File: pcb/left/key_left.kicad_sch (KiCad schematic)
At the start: 106 parts, among them J1 Conn01_02, J3 USB_C_Receptacle_USB2.0_16P, J4 Conn_01x06_Socket, J5 Conn_01x04_Pin, SW1 SW_Push, SW10 SW_Push, SW11 SW_Push, SW12 SW_Push, SW13 SW_Push, SW14 SW_Push, SW15 SW_Push, SW16 SW_Push, SW17 SW_Push, SW18 SW_Push, SW19 SW_Push, SW2 SW_Push, SW20 SW_Push, SW21 SW_Push, SW22 SW_Push, SW23 SW_Push, SW3 SW_Push, SW4 SW_Push, SW5 SW_Push, SW6 SW_Push, SW7 SW_Push, SW8 SW_Push, SW9 SW_Push, U2 MDBT50Q-1MV2, U3 IS31FL3733-TQ, U4 BQ24074RGT

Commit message: ERC verified and symbols are added
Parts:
- C29, C30, C31, C6, C8, C9: footprint (none) -> Capacitor_SMD:C_0805_2012Metric
- D24, D25, D26, D27, D28, D30, D31, D32, D33, D34, D36, D37, D38, D39, D40, D41, D42, D43, D44, D45, D46, D47, D48, D50: footprint (none) -> LED_SMD:LED_RGB_5050-6; symbol Device:LED_RGB -> LED_RGB_5050:LED_RGB_5050
- R1, R10, R11, R12, R13, R14, R15, R16, R17, R18, R19, R4, R7, R8, R9: footprint (none) -> Resistor_SMD:R_0805_2012Metric
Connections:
- net CS1: now also D24.2 (RK), D30.2 (RK), D36.2 (RK), D41.2 (RK), D46.2 (RK); no longer D24.1 (RK), D30.1 (RK), D36.1 (RK), D41.1 (RK), D46.1 (RK)
- net CS10: now also D27.2 (RK), D33.2 (RK), D39.2 (RK), D44.2 (RK); no longer D27.1 (RK), D33.1 (RK), D39.1 (RK), D44.1 (RK)
- net CS11: now also D27.3 (GK), D33.3 (GK), D39.3 (GK), D44.3 (GK); no longer D27.2 (GK), D33.2 (GK), D39.2 (GK), D44.2 (GK)
- net CS12: now also D27.1 (BK), D33.1 (BK), D39.1 (BK), D44.1 (BK); no longer D27.3 (BK), D33.3 (BK), D39.3 (BK), D44.3 (BK)
- net CS13: now also D28.2 (RK), D34.2 (RK), D40.2 (RK), D45.2 (RK); no longer D28.1 (RK), D34.1 (RK), D40.1 (RK), D45.1 (RK)
- net CS14: now also D28.3 (GK), D34.3 (GK), D40.3 (GK), D45.3 (GK); no longer D28.2 (GK), D34.2 (GK), D40.2 (GK), D45.2 (GK)
- net CS15: now also D28.1 (BK), D34.1 (BK), D40.1 (BK), D45.1 (BK); no longer D28.3 (BK), D34.3 (BK), D40.3 (BK), D45.3 (BK)
- net CS2: now also D24.3 (GK), D30.3 (GK), D36.3 (GK), D41.3 (GK), D46.3 (GK); no longer D24.2 (GK), D30.2 (GK), D36.2 (GK), D41.2 (GK), D46.2 (GK)
- net CS3: now also D24.1 (BK), D30.1 (BK), D36.1 (BK), D41.1 (BK), D46.1 (BK); no longer D24.3 (BK), D30.3 (BK), D36.3 (BK), D41.3 (BK), D46.3 (BK)
- net CS4: now also D25.2 (RK), D31.2 (RK), D37.2 (RK), D42.2 (RK), D47.2 (RK); no longer D25.1 (RK), D31.1 (RK), D37.1 (RK), D42.1 (RK), D47.1 (RK)
- net CS5: now also D25.3 (GK), D31.3 (GK), D37.3 (GK), D42.3 (GK), D47.3 (GK); no longer D25.2 (GK), D31.2 (GK), D37.2 (GK), D42.2 (GK), D47.2 (GK)
- net CS6: now also D25.1 (BK), D31.1 (BK), D37.1 (BK), D42.1 (BK), D47.1 (BK); no longer D25.3 (BK), D31.3 (BK), D37.3 (BK), D42.3 (BK), D47.3 (BK)
- net CS7: now also D26.2 (RK), D32.2 (RK), D38.2 (RK), D43.2 (RK), D48.2 (RK); no longer D26.1 (RK), D32.1 (RK), D38.1 (RK), D43.1 (RK), D48.1 (RK)
- net CS8: now also D26.3 (GK), D32.3 (GK), D38.3 (GK), D43.3 (GK), D48.3 (GK); no longer D26.2 (GK), D32.2 (GK), D38.2 (GK), D43.2 (GK), D48.2 (GK)
- net CS9: now also D26.1 (BK), D32.1 (BK), D38.1 (BK), D43.1 (BK), D48.1 (BK); no longer D26.3 (BK), D32.3 (BK), D38.3 (BK), D43.3 (BK), D48.3 (BK)
- net GND: now also J3.SH (SHIELD); no longer J3.S1 (SHIELD)
- net at R16.1: now also D50.2 (RK); no longer D50.1 (RK)
- net at R14.1: now also D50.1 (BK); no longer D50.3 (BK)
- net at R15.2: now also D50.3 (GK); no longer D50.2 (GK)
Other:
- moved on the sheet: C6, C8, C9, J3, R11, R12, R13, R17, R18, R19, R2, R3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

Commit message: SWD firmware debug unit added
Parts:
- added C1: 1uF, symbol Device:C
- added C2, C3, C4: 100nF, symbol Device:C
- added C5: C, symbol Device:C
- added LDO1: ME6211C33M5G-N, easyeda2kicad:SOT-23-5_L3.0-W1.7-P0.95-LS2.8-BL, symbol easyeda2kicad:ME6211C33M5G-N
- added Q1: AO3401A, easyeda2kicad:SOT-23_L2.9-W1.3-P1.90-LS2.4-BR, symbol easyeda2kicad:AO3401A
- added Q2: 2N7002, easyeda2kicad:SOT-23-3_L2.9-W1.3-P1.90-LS2.4-BR, symbol easyeda2kicad:2N7002
- added R20: 100 k, symbol Device:R
- added R21, R22: 100k, symbol Device:R
- added SW24: SW_Push, symbol Switch:SW_Push
- added U1: CH552E, easyeda2kicad:MSOP-10_L3.0-W3.0-P0.50-LS5.0-BL, symbol easyeda2kicad:CH552E
- added U5: FSUSB42UMX-TP, easyeda2kicad:XQFN-10_L1.8-W1.4-P0.40-TL, symbol easyeda2kicad:FSUSB42UMX-TP
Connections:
- net +5V: now also C3.2, LDO1.1 (VIN), LDO1.3 (CE), Q1.2 (S), R21.2
- net GND: now also C1.1, C2.1, C3.1, C4.2, C5.2, LDO1.2 (VSS), Q1.3 (D), Q2.1 (G), Q2.2 (S), R20.2, R22.2, SW24.2, U1.8 (GND/VSS), U5.3 (GND), U5.8 (~{OE})
- net USB_D+: now also U5.1 (D+); no longer U2.35 (D+)
- net USB_D-: now also U5.2 (D-); no longer U2.34 (D-)
- net NRST: now reaches U2.40 (P0.18)
- net NRST: now also U1.3 (P1.6/MISO/RXD1/TIN4)
- net at J5.1 (Pin_1): no longer U2.51 (SWDIO)
- net at J5.2 (Pin_2): no longer U2.53 (SWDCLK)
- new net: R22.1, U1.4 (P1.7/SCK/TXD1/TIN5)
- new net: C4.1, U1.9 (VCC/VDD)
- new net +3V3F: C1.2, C2.2, LDO1.5 (VOUT), U5.9 (VCC)
- new net CH_D+: U1.6 (P3.6/UDP), U5.7 (HSD2+)
- new net CH_D-: U1.7 (P3.7/UDM), U5.6 (HSD2-)
- new net CH_V33: C5.1, R20.1, U1.10 (V33), U5.10 (SEL)
- new net GATE: Q1.1 (G), Q2.3 (D), R21.1, SW24.1
- new net NRF_D+: U2.35 (D+), U5.5 (HSD1+)
- new net NRF_D-: U2.34 (D-), U5.4 (HSD1-)
- new net SWCLK: U1.1 (P1.4/T2_/CAP1_/SCS/TIN2/UCC1/AIN1), U2.53 (SWDCLK)
- new net SWDIO: U1.2 (P1.5/MOSI/PWM1/TIN3/UCC2/AIN2), U2.51 (SWDIO)
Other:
- moved on the sheet: C10, C29, C30, C31, C6, C8, C9, D1, D10, D11, D12, D13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

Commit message: Firmware reset button added
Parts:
- removed J1: Conn01_02, Connector_JST:JST_PH_B2B-PH-K_1x02_P2.00mm_Vertical, symbol Connector:Conn_01x02_Socket
- removed J5: Conn_01x04_Pin, Connector_PinHeader_2.54mm:PinHeader_1x04_P2.54mm_Vertical, symbol Connector:Conn_01x04_Pin
- removed R2, R3: 5.1k, Resistor_SMD:R_0805_2012Metric, symbol Device:R_Small
- removed R7: 10k, Resistor_SMD:R_0805_2012Metric, symbol Device:R
- added C12, C13, C14, C15, C16, C17, C18: 100nF, symbol Device:C
- added J1: Conn_01x03_Socket, symbol Connector:Conn_01x03_Socket
- added Q3, Q4: 2N7002, easyeda2kicad:SOT-23-3_L2.9-W1.3-P1.90-LS2.4-BR, symbol easyeda2kicad:2N7002
- added R2: 887k, symbol Device:R
- added R23, R25, R26, R27, R3: 10k, symbol Device:R
- added R24: 100k, symbol Device:R
- added SW25: SW_Push, symbol Switch:SW_Push
- added U6: SN74LVC1T45DBV, Package_TO_SOT_SMD:SOT-23-6, symbol Logic_LevelTranslator:SN74LVC1T45DBV
- added U7: TUSB320, Package_DFN_QFN:Texas_X2QFN-12_1.6x1.6mm_P0.4mm, symbol Interface_USB:TUSB320
- added U8: TXS0101DBV, Package_TO_SOT_SMD:SOT-23-6, symbol Logic_LevelTranslator:TXS0101DBV
- C10, C7: value 1uF -> 10µF
- C11: value 4.7uF -> 10µF
- C3: value 100nF -> 1uF
- C5: value C -> 100nF
- R4: value 1M -> 470k
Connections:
- net +3V3F: now also C17.1, R26.1, R3.2, U7.12 (VDD)
- net +5V: now also C10.1, R2.2
- net +BATT: now also U4.[2,3] (BAT), J1.1 (Pin_1); no longer U4.2 (BAT)
- net 3V3: now also C14.1, C16.1, R23.2, R25.2, R27.1, U6.6 (VCCB), U8.1 (V_{CCA}), U8.5 (OE); no longer C10.2, U3.46 (~{SDB}), U4.5 (EN2)
- net BAT_SENSE: now also C18.1
- net GND: now also C10.2, C12.2, C13.2, C14.2, C15.2, C16.2, C17.2, C18.2, J1.2 (Pin_2), Q3.2 (S), Q4.2 (S), R24.2, SW25.2, U6.2 (GND), U7.10 (GND), U7.11 (~{EN}), U7.3 (PORT), U8.2 (GND); no longer C10.1, Q1.3 (D), Q2.1 (G), U4.6 (EN1)
- net VCC_SYS: now also U4.[10,11] (OUT); no longer U4.10 (OUT)
- net BATT_NTC: now reaches U4.1 (TS)
- net BATT_NTC: now also J1.3 (Pin_3)
- net USB_CC2: now reaches J3.B5 (CC2)
- net USB_CC2: now also U7.2 (CC2)
- net PWR_BTN: now reaches U2.12 (P0.31)
- net PWR_BTN: now also C12.1, R23.1, SW25.1
- net KEEPON: now reaches R22.1, U1.4 (P1.7/SCK/TXD1/TIN5)
- net KEEPON: now also Q2.1 (G)
- net USB_CC1: now reaches J3.A5 (CC1)
- net USB_CC1: now also U7.1 (CC1)
- net CH_VCC: now reaches C4.1, U1.9 (VCC/VDD)
- net CH_VCC: now also Q1.3 (D), C13.1, C15.1, U6.1 (VCCA), U6.5 (DIR), U8.6 (V_{CCB})
- net NRST renamed CH_NRST_CTRL
- net CH_NRST_CTRL: now also Q3.1 (G), R24.1; no longer U2.40 (P0.18)
- net SWCLK renamed CH_SWCLK
- net CH_SWCLK: now also U6.3 (A); no longer U2.53 (SWDCLK)
- net SWDIO renamed CH_SWDIO
- net CH_SWDIO: now also U8.4 (B); no longer U2.51 (SWDIO)
- new net: R2.1, U7.4 (VBUS_DET)
- new net: R27.2, U3.46 (~{SDB})
- new net BQ_EN2: Q4.3 (D), R26.2, U4.5 (EN2)
- new net NRF_NRST: Q3.3 (D), R25.1, U2.40 (P0.18)
- new net NRF_SWCLK: U2.53 (SWDCLK), U6.4 (B)
- new net NRF_SWDIO: U2.51 (SWDIO), U8.3 (A)
- new net TYPEC_OUT1: Q4.1 (G), R3.1, U4.6 (EN1), U7.7 (SDA/OUT1)
- no-connect marks 38 -> 42
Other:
- note added: "BQ24074 Current Mode Select"
- note added: "CH552 3V3 Regulator"
- note added: "CH552 Decoupling"
- note added: "CH552 Power Latch"
- note added: "CH552 Power Switch"
- note added: "CH552 Program Button"
- note added: "CH552 Programmer"
- note added: "IS31FL3733 Controller"
- note added: "Power / Pair Button"
- note added: "SWDCLK Level Shifter"
- note added: "SWDIO Level Shifter"
- note added: "Switch matrix"
- note added: "USB Data Mux"
- note added: "USB-C Current Detection"
- note added: "nRF Reset Level Protection"
- note added: "nRF52840 Controller"
- note removed: "Controller"
- note removed: "LED Controller"
- note removed: "Left Switch matrix"
- moved on the sheet: C1, C11, C2, C3, C4, C5, C6, C7, C8, C9, D1, D10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

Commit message: Trackpad removed for now upon release of version 1.0
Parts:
- removed J4: Conn_01x06_Socket, Connector_FFC-FPC:TE_84953-6_1x06-1MP_P1.0mm_Horizontal, symbol Connector:Conn_01x06_Socket
- removed R5, R6: 4.7k, Resistor_SMD:R_0805_2012Metric, symbol Device:R
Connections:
- net TRACKPAD_INT: no longer names the net of U2.48 (P0.24)
- net TRACKPAD_RST: no longer names the net of U2.49 (P0.25)
- net TRACKPAD_SCL: no longer names the net of U2.45 (P0.23)
- net TRACKPAD_SDA: no longer names the net of U2.46 (P0.22)
- no-connect marks 42 -> 46
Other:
- note removed: "TrackPad"
- moved on the sheet: C12, C18, Q4, R1, R23, R26, R4, SW25

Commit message: Decouplers and CH552 bootloader reset added
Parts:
- removed C30: 100nF, Capacitor_SMD:C_0805_2012Metric, symbol Device:C
- removed C31: 10uF, Capacitor_SMD:C_0805_2012Metric, symbol Device:C
- removed R27: 10k, symbol Device:R
- added C19, C22, C24, C25: 100nF, symbol Device:C
- added C20, C21, C23: 470nF, symbol Device:C
- added R5: 100k, symbol Device:R
- added R6: 10k, symbol Device:R
- added SW26: SW_BOOT, symbol Switch:SW_Push
- C29: value 100nF -> 470nF
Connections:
- net 3V3: no longer U3.38 (DVCC)
- net CH_D+: now also R6.1
- net CH_V33: now also C25.2, SW26.2
- net GND: now also C19.2, C20.2, C21.2, C22.2, C23.2, C24.2, C25.1, R5.1
- net LED_EN: now reaches U2.13 (P0.28)
- net LED_EN: now also U3.46 (~{SDB}), R5.2
- net VCC_SYS renamed AVCC_DVCC
- net AVCC_DVCC: now also U3.38 (DVCC), C19.1, C20.1, C21.1, C22.1, C23.1, C24.1
- new net: R6.2, SW26.1
- no-connect marks 46 -> 45
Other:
- note added: "IS31FL3733 decouplers"
- moved on the sheet: C17, C29, C4, R10, R2, R3, R8, R9, U3, U7

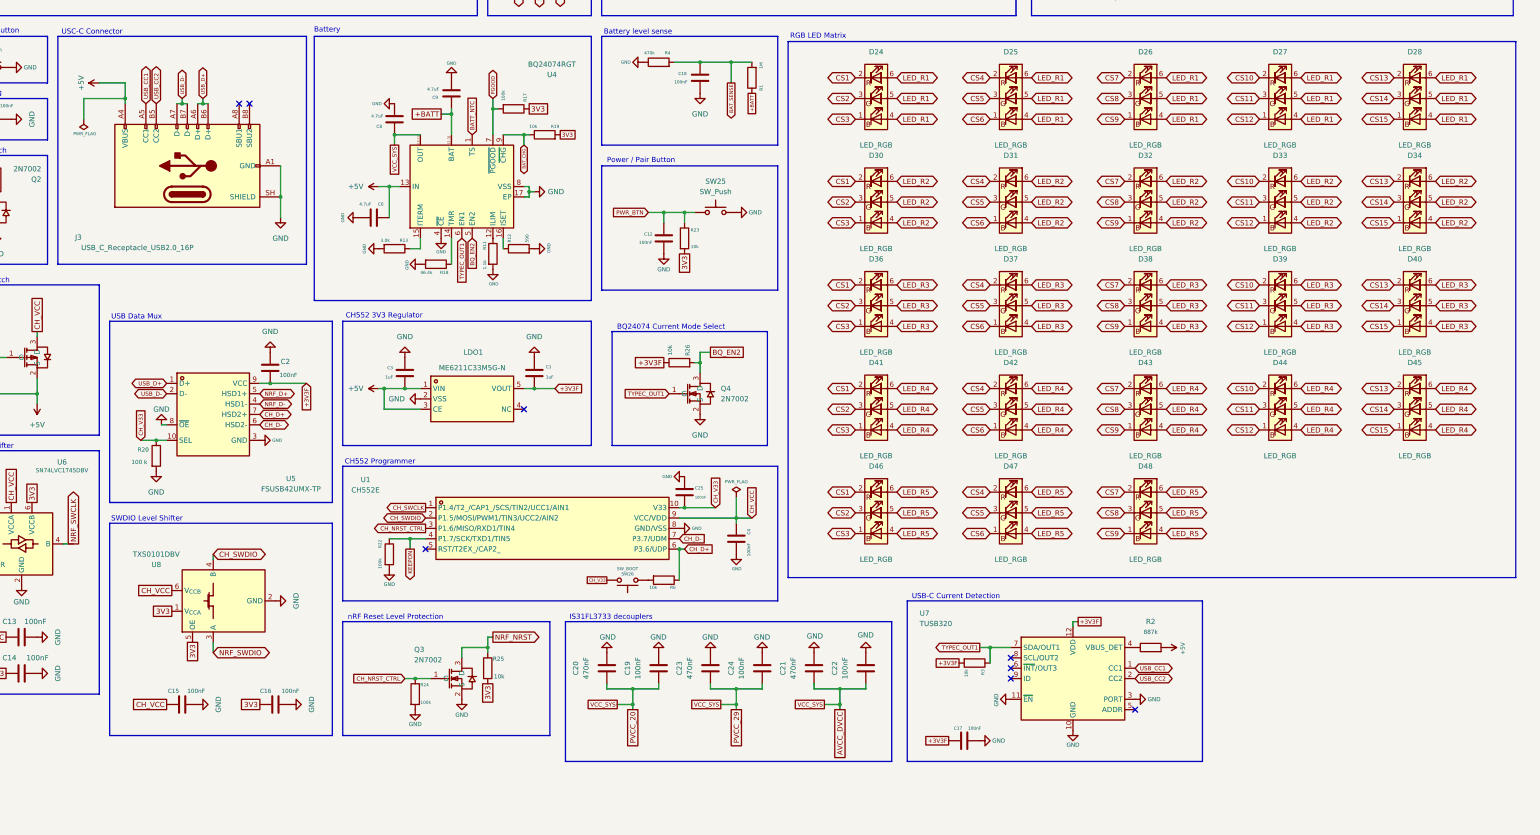
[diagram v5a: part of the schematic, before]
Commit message: USB ESD Protection Added
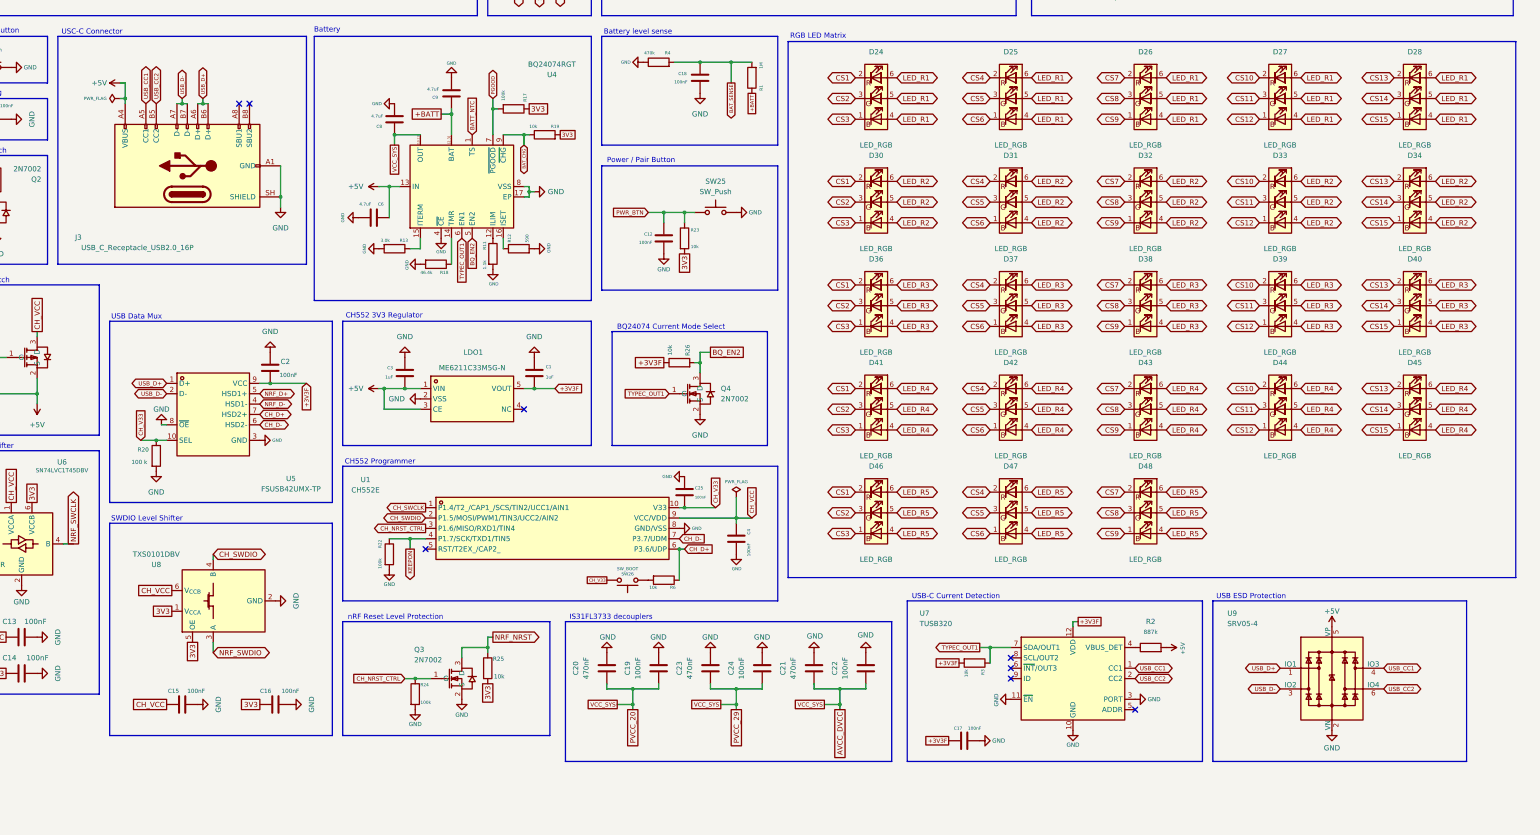
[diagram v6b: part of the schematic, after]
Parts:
- added U9: SRV05-4, Package_TO_SOT_SMD:SOT-23-6, symbol Power_Protection:SRV05-4
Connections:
- net +5V: now also U9.5 (VP)
- net GND: now also U9.2 (VN)
- net USB_CC1: now also U9.4 (IO3)
- net USB_CC2: now also U9.6 (IO4)
- net USB_D+: now also U9.1 (IO1)
- net USB_D-: now also U9.3 (IO2)
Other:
- note added: "USB ESD Protection"

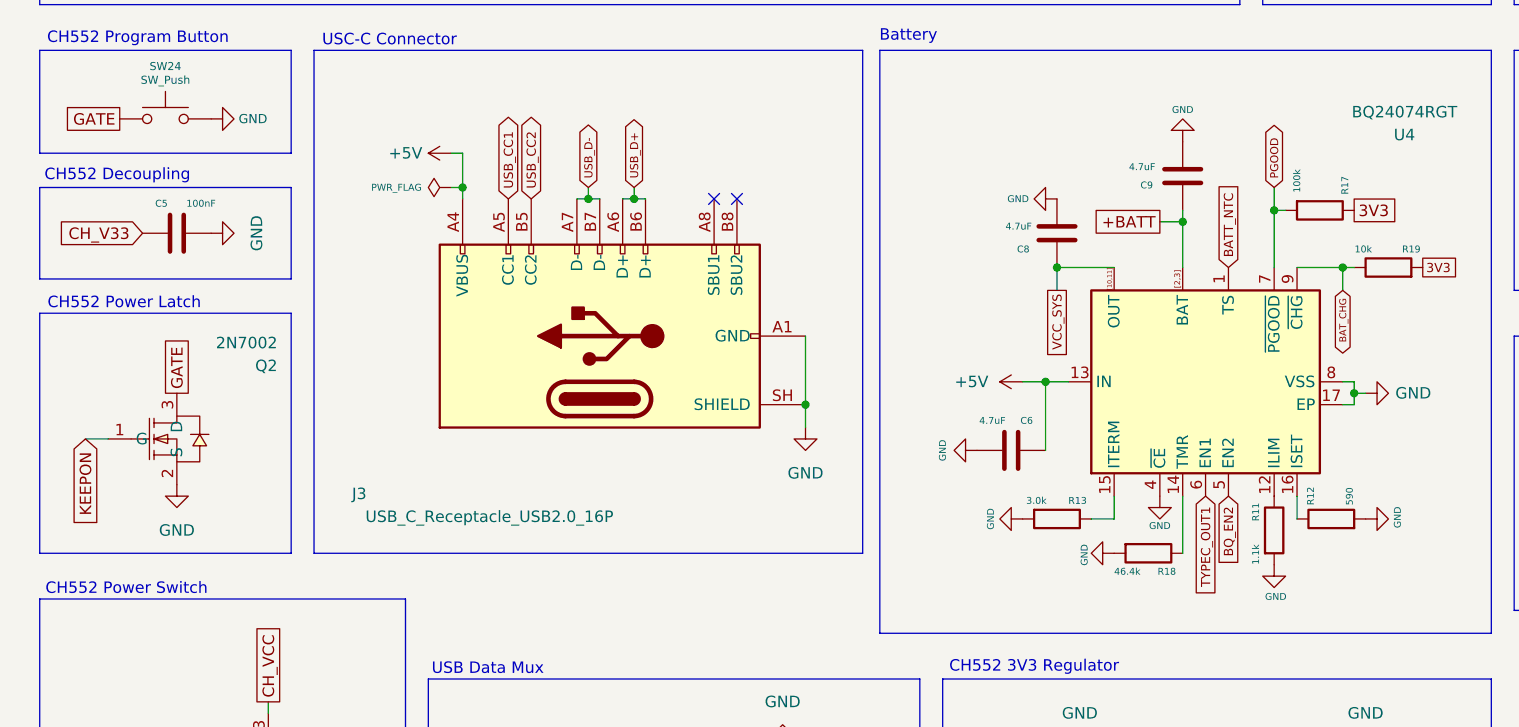
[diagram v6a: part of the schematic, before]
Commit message: IS31FL3733 Bulk Decoupling added
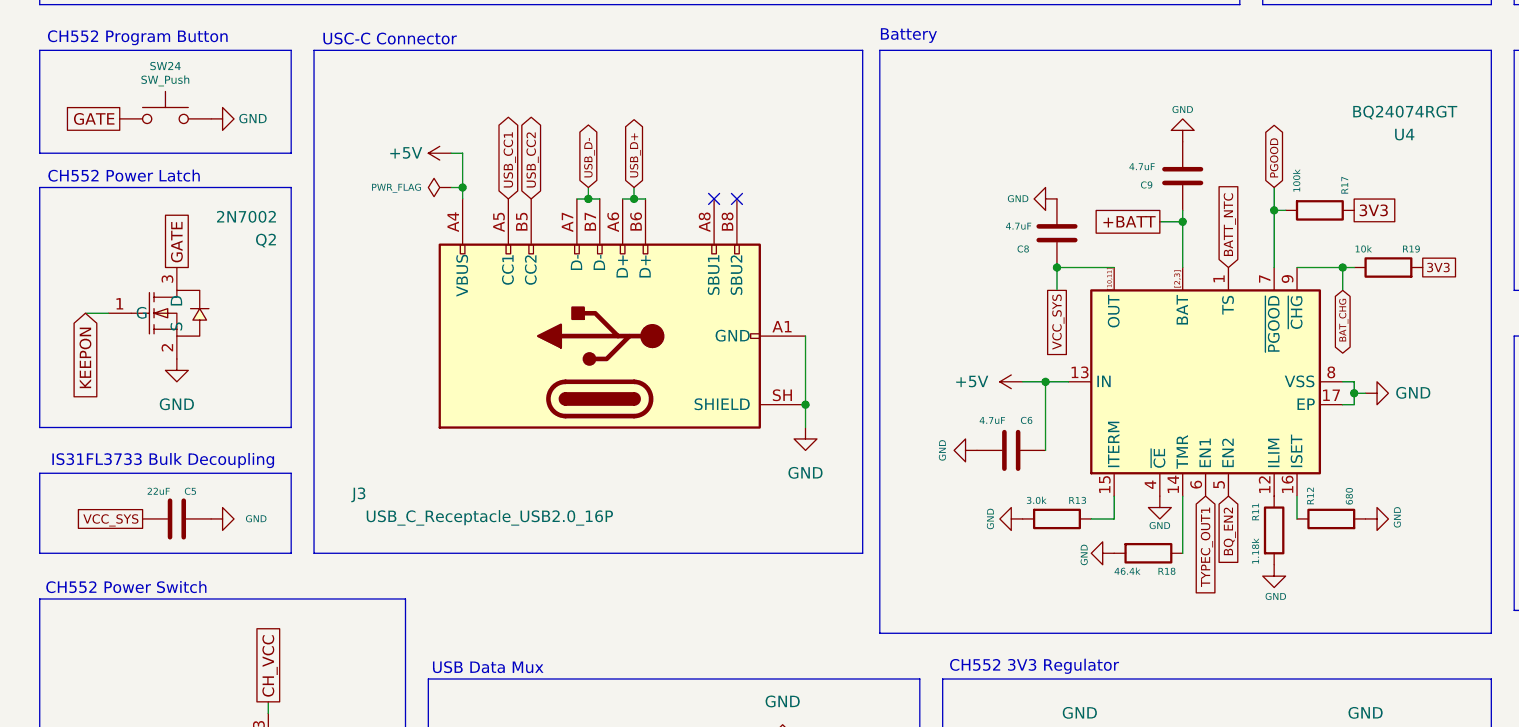
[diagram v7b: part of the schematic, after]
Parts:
- C5: value 100nF -> 22uF
- R11: value 1.1k -> 1.18k
- R12: value 590 -> 680
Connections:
- net AVCC_DVCC: now also C5.1
- net CH_V33: no longer C5.1
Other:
- note added: "IS31FL3733 Bulk Decoupling"
- note removed: "CH552 Decoupling"
- moved on the sheet: Q2
